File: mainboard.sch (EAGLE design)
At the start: 121 parts, among them X1 FH12-24S-0.5SH, X3 87438-02

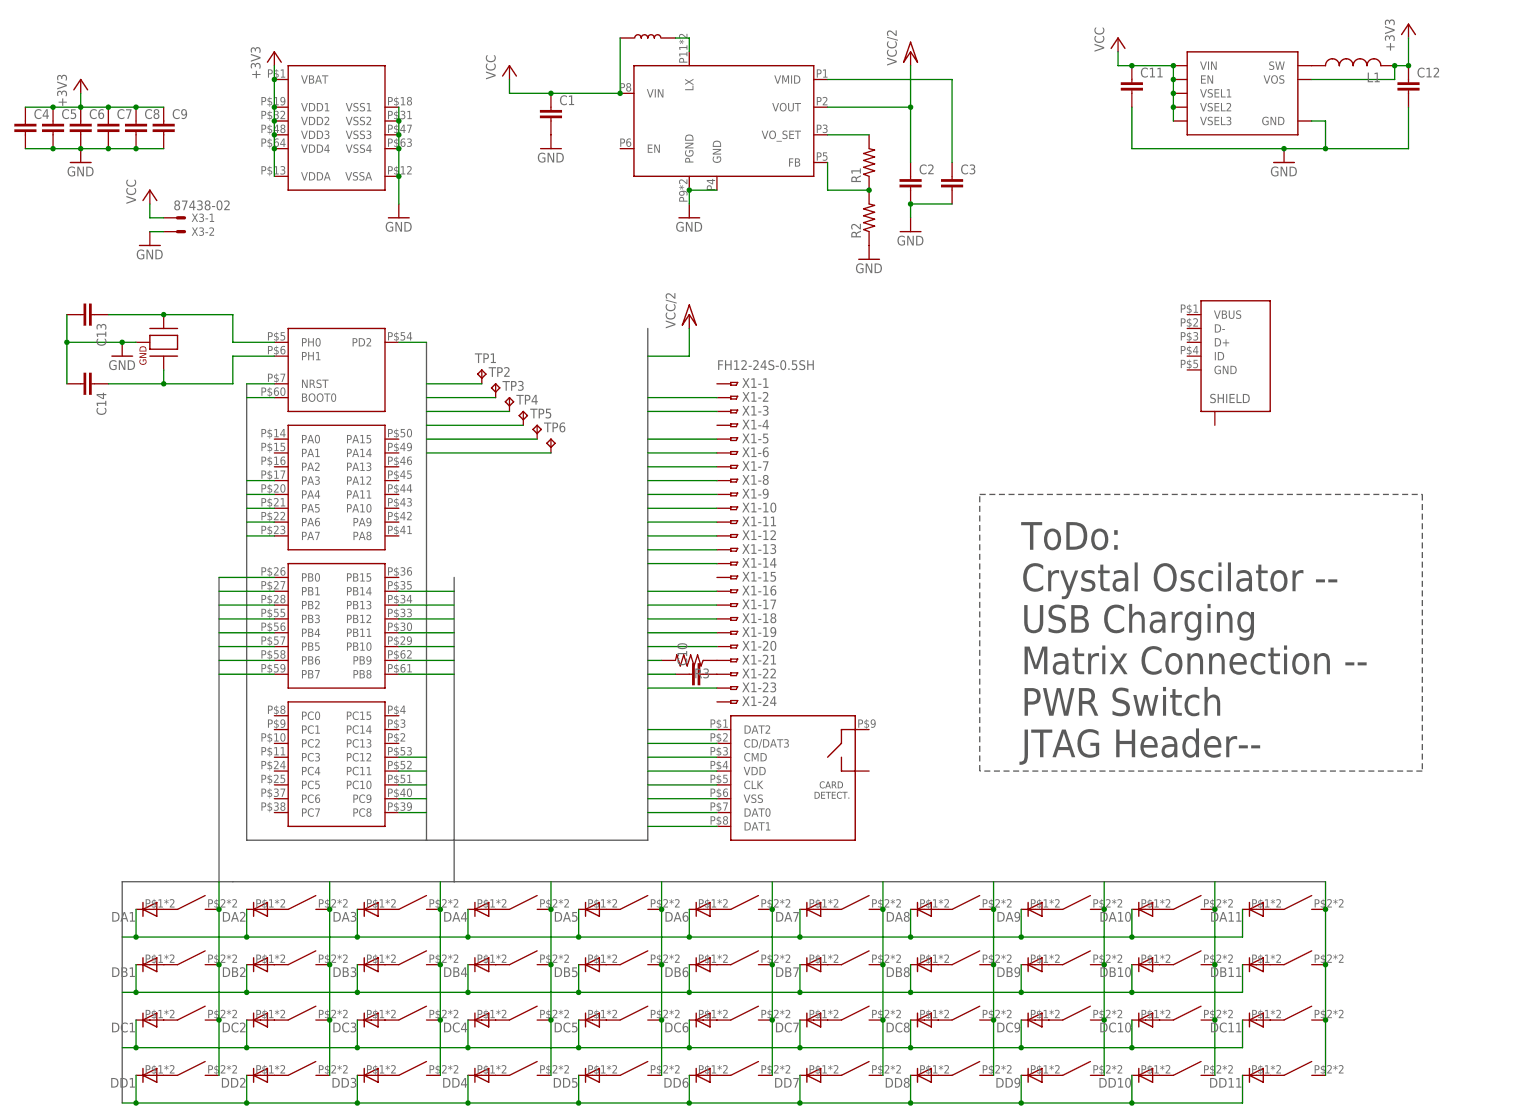
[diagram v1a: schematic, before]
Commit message: [Rev1] Finished shematic design
Added usb charging
PWR Button
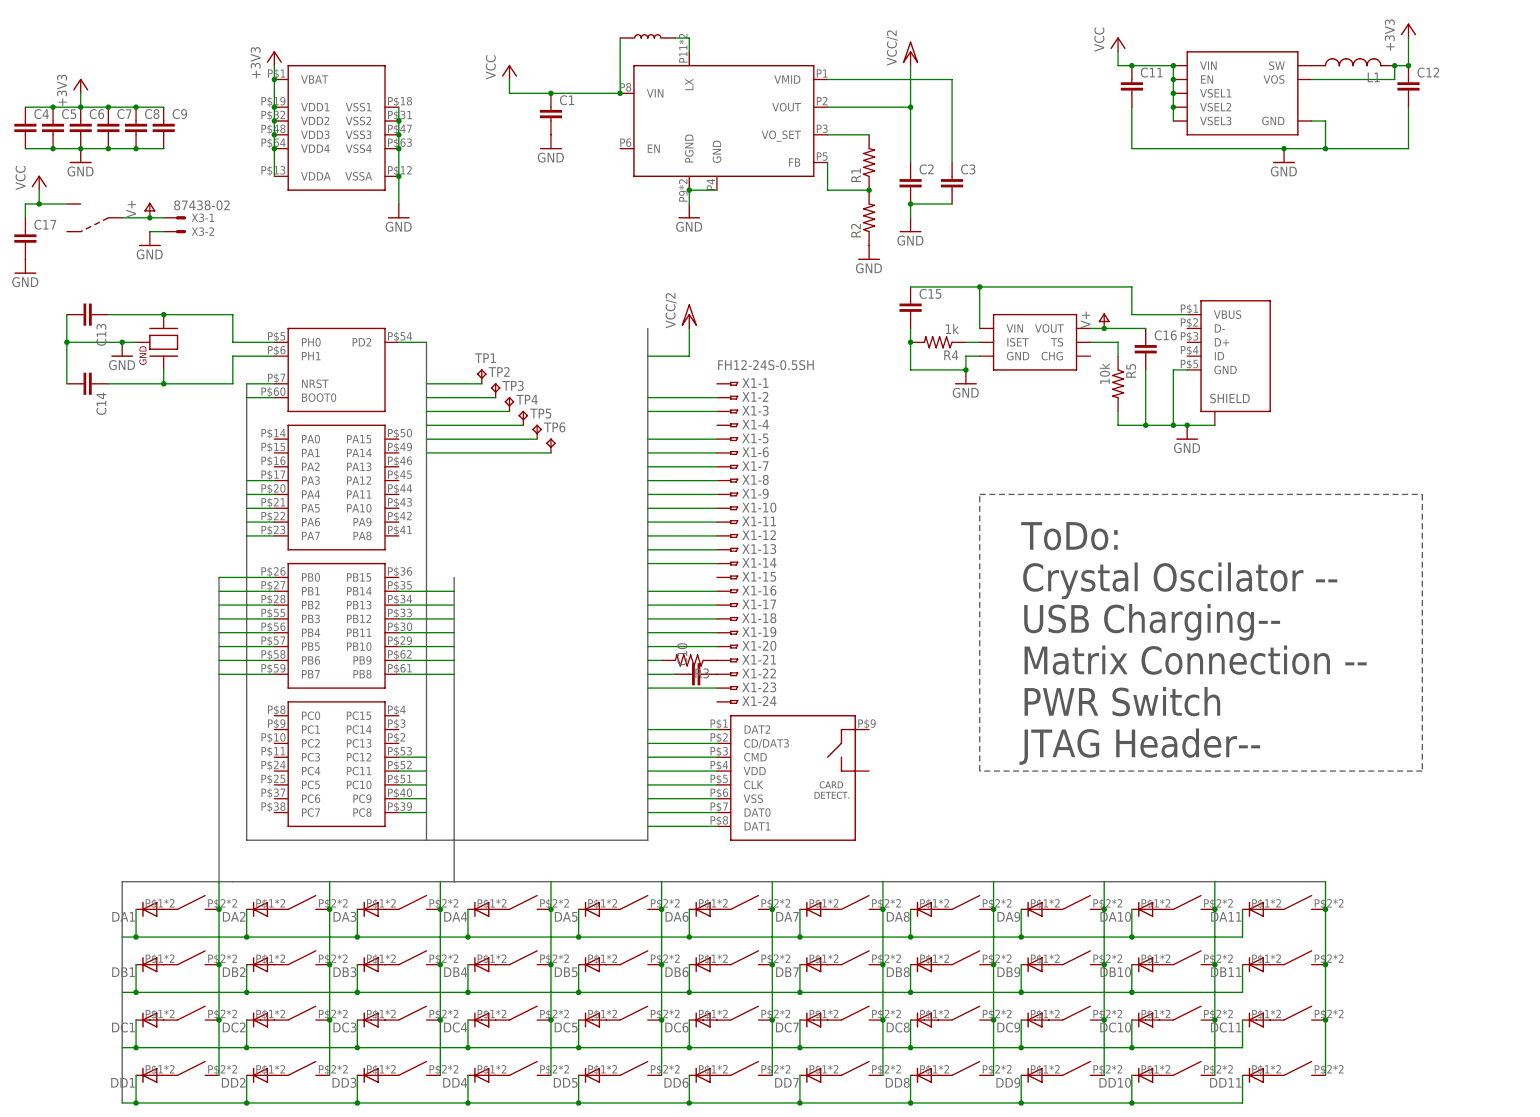
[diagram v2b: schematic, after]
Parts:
- added C15, C16: (no value), rcl:C-EUC0603
- added C17: (no value), eagle-ltspice:CC1206
- added R4: 1k, resistor:R-US_R0402
- added R5: 10k, resistor:R-US_R0402
- added U$8: BQ21040DBVR, lib:BQ21040DBVR
- added U$9: ALPS_SSSS810701, lib:ALPS_SSSS810701
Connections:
- new net N$54: C15.1, U$3.VBUS, U$8.VIN
- new net N$55: R5.1, U$8.TS
- new net N$56: R4.1, U$8.ISET
- new net V+: C16.1, U$8.VOUT, U$9.COM, X3-1.S
- net GND: now also C15.2, C16.2, C17.2, R4.2, R5.2, U$3.GND, U$3.P$6, U$8.GND
- net VCC: now also C17.1, U$9.L; no longer X3-1.S
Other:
- note added: "ToDo: Crystal Oscilator -- USB Charging-- Matrix Connection -- PWR Switch JTAG Header--"
- note removed: "ToDo: Crystal Oscilator -- USB Charging Matrix Connection -- PWR Switch JTAG Header--"
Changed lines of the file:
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@@
 <part name="TP5" library="testpad" deviceset="TP" device="TP20SQ"/>
 <part name="TP6" library="testpad" deviceset="TP" device="TP20SQ"/>
+<part name="U$8" library="lib" deviceset="BQ21040DBVR" device=""/>
+<part name="GND10" library="supply1" deviceset="GND" device=""/>
+<part name="GND11" library="supply1" deviceset="GND" device=""/>
+<part name="R4" library="resistor" deviceset="R-US_" device="R0402" value="1k"/>
+<part name="R5" library="resistor" deviceset="R-US_" device="R0402" value="10k"/>
+<part name="C15" library="rcl" deviceset="C-EU" device="C0603"/>
+<part name="C16" library="rcl" deviceset="C-EU" device="C0603"/>
+<part name="P+7" library="supply1" deviceset="V+" device=""/>
+<part name="P+8" library="supply1" deviceset="V+" device=""/>
+<part name="U$9" library="lib" deviceset="ALPS_SSSS810701" device=""/>
+<part name="C17" library="eagle-ltspice" deviceset="C" device="C1206"/>
+<part name="GND12" library="supply1" deviceset="GND" device=""/>
 </parts>
 <sheets>
@@
 <text x="170.18" y="66.04" size="5.08" layer="97">ToDo:
 Crystal Oscilator --
-USB Charging
+USB Charging--
 Matrix Connection --
 PWR Switch
@@
 <instance part="C10" gate="G$1" x="109.22" y="81.28" rot="R90"/>
 <instance part="P+3" gate="G$1" x="109.22" y="147.32"/>
-<instance part="P+4" gate="VCC" x="10.16" y="170.18"/>
+<instance part="P+4" gate="VCC" x="-10.16" y="172.72"/>
 <instance part="GND7" gate="1" x="10.16" y="160.02"/>
 <instance part="C4" gate="G$1" x="-12.7" y="182.88"/>
@@
 <instance part="TP5" gate="G$1" x="81.28" y="127"/>
 <instance part="TP6" gate="G$1" x="83.82" y="124.46"/>
+<instance part="U$8" gate="G$1" x="172.72" y="142.24"/>
+<instance part="GND10" gate="1" x="160.02" y="134.62"/>
+<instance part="GND11" gate="1" x="200.66" y="124.46"/>
+<instance part="R4" gate="G$1" x="154.94" y="142.24" rot="R180"/>
+<instance part="R5" gate="G$1" x="187.96" y="134.62" rot="R270"/>
+<instance part="C15" gate="G$1" x="149.86" y="149.86"/>
+<instance part="C16" gate="G$1" x="193.04" y="142.24"/>
+<instance part="P+7" gate="1" x="10.16" y="167.64"/>
+<instance part="P+8" gate="1" x="185.42" y="147.32"/>
+<instance part="U$9" gate="G$1" x="0" y="165.1" rot="R180"/>
+<instance part="C17" gate="G$1" x="-12.7" y="162.56"/>
+<instance part="GND12" gate="1" x="-12.7" y="154.94"/>
 </instances>
 <busses>
@@
 <pinref part="TP4" gate="G$1" pin="TP"/>
 <wire x1="78.74" y1="127" x2="60.96" y2="127" width="0.1524" layer="91"/>
+</segment>
+<segment>
+<pinref part="GND10" gate="1" pin="GND"/>
+<wire x1="160.02" y1="137.16" x2="160.02" y2="139.7" width="0.1524" layer="91"/>
+<pinref part="U$8" gate="G$1" pin="GND"/>
+<wire x1="160.02" y1="139.7" x2="162.56" y2="139.7" width="0.1524" layer="91"/>
+<pinref part="R4" gate="G$1" pin="2"/>
+<wire x1="149.86" y1="142.24" x2="149.86" y2="137.16" width="0.1524" layer="91"/>
+<wire x1="149.86" y1="137.16" x2="160.02" y2="137.16" width="0.1524" layer="91"/>
+<junction x="160.02" y="137.16"/>
+<pinref part="C15" gate="G$1" pin="2"/>
+<wire x1="149.86" y1="144.78" x2="149.86" y2="142.24" width="0.1524" layer="91"/>
+<junction x="149.86" y="142.24"/>
+</segment>
+<segment>
+<pinref part="U$3" gate="G$1" pin="GND"/>
+<wire x1="200.66" y1="137.16" x2="198.12" y2="137.16" width="0.1524" layer="91"/>
+<wire x1="198.12" y1="137.16" x2="198.12" y2="127" width="0.1524" layer="91"/>
+<pinref part="U$3" gate="G$1" pin="P$6"/>
+<wire x1="198.12" y1="127" x2="200.66" y2="127" width="0.1524" layer="91"/>
+<pinref part="GND11" gate="1" pin="GND"/>
+<wire x1="200.66" y1="127" x2="205.74" y2="127" width="0.1524" layer="91"/>
+<junction x="200.66" y="127"/>
+<pinref part="R5" gate="G$1" pin="2"/>
+<wire x1="187.96" y1="129.54" x2="187.96" y2="127" width="0.1524" layer="91"/>
+<wire x1="187.96" y1="127" x2="193.04" y2="127" width="0.1524" layer="91"/>
+<junction x="198.12" y="127"/>
+<pinref part="C16" gate="G$1" pin="2"/>
+<wire x1="193.04" y1="127" x2="198.12" y2="127" width="0.1524" layer="91"/>
+<wire x1="193.04" y1="137.16" x2="193.04" y2="127" width="0.1524" layer="91"/>
+<junction x="193.04" y="127"/>
+</segment>
+<segment>
+<pinref part="C17" gate="G$1" pin="2"/>
+<pinref part="GND12" gate="1" pin="GND"/>
 </segment>
 </net>
@@
 <wire x1="83.82" y1="187.96" x2="96.52" y2="187.96" width="0.1524" layer="91"/>
 <junction x="83.82" y="187.96"/>
-</segment>
-<segment>
-<pinref part="P+4" gate="VCC" pin="VCC"/>
-<wire x1="12.7" y1="165.1" x2="10.16" y2="165.1" width="0.1524" layer="91"/>
-<wire x1="10.16" y1="165.1" x2="10.16" y2="167.64" width="0.1524" layer="91"/>
-<pinref part="X3" gate="-1" pin="S"/>
 </segment>
 <segment>
@@
 <pinref part="C11" gate="G$1" pin="1"/>
 <junction x="190.5" y="193.04"/>
+</segment>
+<segment>
+<pinref part="P+4" gate="VCC" pin="VCC"/>
+<wire x1="-10.16" y1="170.18" x2="-10.16" y2="167.64" width="0.1524" layer="91"/>
+<pinref part="C17" gate="G$1" pin="1"/>
+<wire x1="-12.7" y1="165.1" x2="-12.7" y2="167.64" width="0.1524" layer="91"/>
+<wire x1="-12.7" y1="167.64" x2="-10.16" y2="167.64" width="0.1524" layer="91"/>
+<pinref part="U$9" gate="G$1" pin="L"/>
+<wire x1="-10.16" y1="167.64" x2="-5.08" y2="167.64" width="0.1524" layer="91"/>
+<junction x="-10.16" y="167.64"/>
 </segment>
 </net>
@@
 </segment>
 </net>
+<net name="N$54" class="0">
+<segment>
+<pinref part="U$3" gate="G$1" pin="VBUS"/>
+<wire x1="200.66" y1="147.32" x2="190.5" y2="147.32" width="0.1524" layer="91"/>
+<wire x1="190.5" y1="147.32" x2="190.5" y2="152.4" width="0.1524" layer="91"/>
+<pinref part="U$8" gate="G$1" pin="VIN"/>
+<wire x1="190.5" y1="152.4" x2="162.56" y2="152.4" width="0.1524" layer="91"/>
+<wire x1="162.56" y1="152.4" x2="162.56" y2="144.78" width="0.1524" layer="91"/>
+<pinref part="C15" gate="G$1" pin="1"/>
+<wire x1="162.56" y1="152.4" x2="149.86" y2="152.4" width="0.1524" layer="91"/>
+<junction x="162.56" y="152.4"/>
+</segment>
+</net>
+<net name="N$56" class="0">
+<segment>
+<pinref part="U$8" gate="G$1" pin="ISET"/>
+<pinref part="R4" gate="G$1" pin="1"/>
+<wire x1="162.56" y1="142.24" x2="160.02" y2="142.24" width="0.1524" layer="91"/>
+</segment>
+</net>
+<net name="N$55" class="0">
+<segment>
+<pinref part="U$8" gate="G$1" pin="TS"/>
+<pinref part="R5" gate="G$1" pin="1"/>
+<wire x1="182.88" y1="142.24" x2="187.96" y2="142.24" width="0.1524" layer="91"/>
+<wire x1="187.96" y1="142.24" x2="187.96" y2="139.7" width="0.1524" layer="91"/>
+</segment>
+</net>
+<net name="V+" class="0">
+<segment>
+<pinref part="U$8" gate="G$1" pin="VOUT"/>
+<pinref part="C16" gate="G$1" pin="1"/>
+<wire x1="193.04" y1="144.78" x2="185.42" y2="144.78" width="0.1524" layer="91"/>
+<pinref part="P+8" gate="1" pin="V+"/>
+<wire x1="185.42" y1="144.78" x2="182.88" y2="144.78" width="0.1524" layer="91"/>
+<junction x="185.42" y="144.78"/>
+</segment>
+<segment>
+<pinref part="P+7" gate="1" pin="V+"/>
+<pinref part="X3" gate="-1" pin="S"/>
+<wire x1="10.16" y1="165.1" x2="12.7" y2="165.1" width="0.1524" layer="91"/>
+<pinref part="U$9" gate="G$1" pin="COM"/>
+<wire x1="5.08" y1="165.1" x2="10.16" y2="165.1" width="0.1524" layer="91"/>
+<junction x="10.16" y="165.1"/>
+</segment>
+</net>
